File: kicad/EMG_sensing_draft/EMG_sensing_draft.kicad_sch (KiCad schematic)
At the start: 95 parts, among them J1 USB_A_0480370001, J2 EMG_SIGNAL, J3 DEBUG, U1 MCP6N11-002E/SN, U2 W25Q128JV, U3 ISL90462WIH627Z-TKCT-ND, U4 RP2040, U5 RN4871-I/RM140, U6 Opamp_MCP6024T-E/ST, U7 MCP1702T-3302E_CB, U8 MCP6021, U9 MCP6024T-E/ST, Y1 12MHz

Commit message: Edited multi-unit component
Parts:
- removed C20: 1uF, Capacitor_SMD:C_0603_1608Metric, symbol Device:C
- removed C21: 0.1uF, Capacitor_SMD:C_0603_1608Metric, symbol Device:C
- removed C22: 10uF, Capacitor_SMD:C_0603_1608Metric, symbol Device:C
- removed C23, C29: .33uF, Capacitor_SMD:C_0603_1608Metric, symbol Device:C
- removed C26: .033uF, Capacitor_SMD:C_0603_1608Metric, symbol Device:C
- removed D10, D9: D, symbol Device:D
- removed R19: 787, Resistor_SMD:R_0603_1608Metric, symbol Device:R
- removed R21, R36: 453, Resistor_SMD:R_0603_1608Metric, symbol Device:R
- removed R22, R34: 909, Resistor_SMD:R_0603_1608Metric, symbol Device:R
- removed R23: 8.1k, Resistor_SMD:R_0603_1608Metric, symbol Device:R
- removed R25: 9.09k, Resistor_SMD:R_0603_1608Metric, symbol Device:R
- removed R33, R37, R39, R40: 10k, symbol Device:R
- removed R38: R, symbol Device:R
- removed U9: MCP6024T-E/ST, MCP6024:MCP6024T, symbol MCP6024:MCP6024T-E/ST
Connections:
- net +1.65V: now also U6.12 (VINB+), U6.3 (VINA+); no longer U6.1 (VINA+), U6.1 (VINB+)
- net +3.3V: now also U6.4 (VDD); no longer U6. (VSS)
- net GND: now also C28.1, R32.1, U6.11 (VSS); no longer U6. (VSS)
- net Vout_1: now also U6.13 (VINB-); no longer D7.2 (A), R17.1
- net Vout_2_neg: now also U6.9 (VINC-); no longer U6.2 (VINC-)
- net Vout_2_pos: now also U6.10 (VINC+); no longer U6.1 (VINC+)
- net Vout_3: now also U6.8 (VOUTC); no longer U6.3 (VOUTC)
- net at R11.2, R12.1: now also U6.1 (VOUTA); no longer U6.3 (VOUTA)
- net at R14.2: now also D7.2 (A), R17.1; no longer U6.2 (VINB-)
- net at D7.1 (K), D8.2 (A): now also U6.14 (VOUTB); no longer U6.3 (VOUTB)
- net at C27.2, R31.2, R35.1: now also U6.7 (VOUTD); no longer C28.1, R32.1, U6.3 (VOUTD)
- net at C28.2, R30.2, R32.2: now also U6.5 (VIND+); no longer U6.1 (VIND+)
- net at C27.1, R29.2, R31.1: now also U6.6 (VIND-); no longer U6.2 (VIND-)
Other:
- note removed: "BANDPASS FILTER, RECTIFICATION, AND LEVEL SHIFTING 2"
- moved on the sheet: C15, C16, C17, C27, C28, C30, D7, D8, R10, R11, R12, R14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

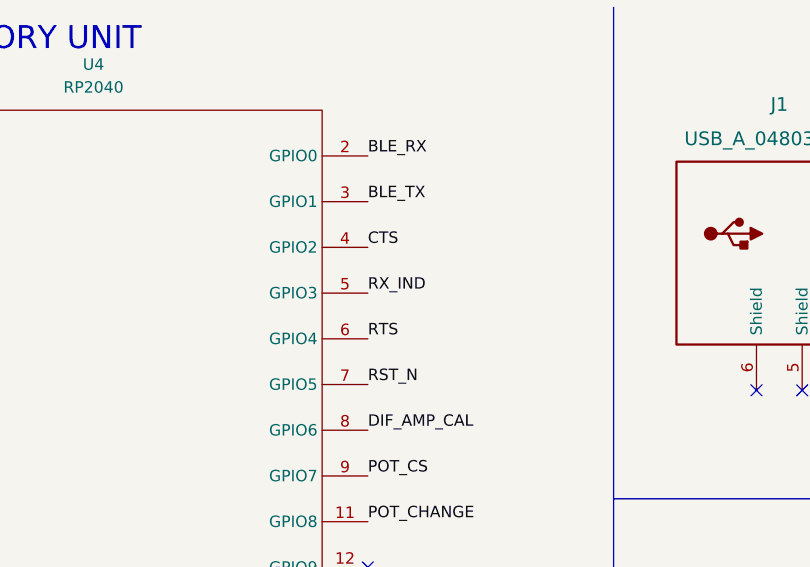
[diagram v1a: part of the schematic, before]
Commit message: fixed ble pins
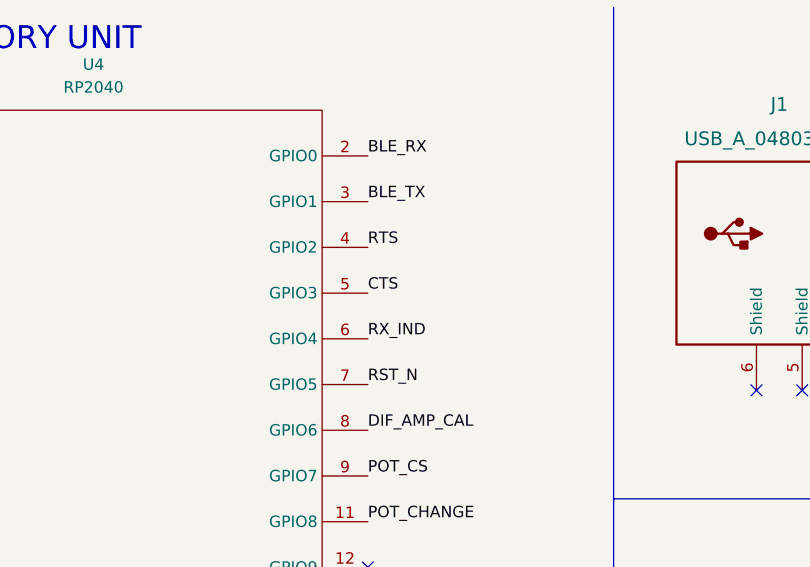
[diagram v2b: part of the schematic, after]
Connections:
- net CTS: now also U4.5 (GPIO3); no longer U4.4 (GPIO2)
- net RTS: now also U4.4 (GPIO2); no longer U4.6 (GPIO4)
- net RX_IND: now also U4.6 (GPIO4); no longer U4.5 (GPIO3)
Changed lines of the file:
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@@
     (effects (font (size 1.27 1.27)) (justify left bottom))
   )
-  (label "RTS" (at 137.16 49.53 0)
+  (label "RTS" (at 137.16 39.37 0)
     (effects (font (size 1.27 1.27)) (justify left bottom))
   )
@@
     (effects (font (size 1.27 1.27)) (justify right bottom))
   )
-  (label "CTS" (at 137.16 39.37 0)
+  (label "CTS" (at 137.16 44.45 0)
     (effects (font (size 1.27 1.27)) (justify left bottom))
   )
@@
     (effects (font (size 1.27 1.27)) (justify right bottom))
   )
-  (label "RX_IND" (at 137.16 44.45 0)
+  (label "RX_IND" (at 137.16 49.53 0)
     (effects (font (size 1.27 1.27)) (justify left bottom))
   )
@@
     (pin "3")
     (pin "10")
+    (pin "8")
     (pin "9")
-    (pin "8")
     (pin "1")
     (pin "2")
@@
     (pin "14")
     (pin "10")
+    (pin "8")
     (pin "9")
-    (pin "8")
     (pin "5")
     (pin "6")
     (pin "7")
+    (pin "11")
     (pin "4")
-    (pin "11")
   )
   (symbol (lib_id "power:+3.3V") (at 72.39 140.97 0) (unit 1)

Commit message: updated footprint assignments
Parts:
- C30: renamed from C25; value .1uF -> 0.1uF
- D7, D8: footprint (none) -> Diode_SMD:D_0805_2012Metric
- R18: renamed from R24; footprint (none) -> Resistor_SMD:R_0603_1608Metric
- R20: renamed from R12; footprint (none) -> Resistor_SMD:R_0603_1608Metric
- R21: renamed from R15; footprint (none) -> Resistor_SMD:R_0603_1608Metric
- R24: renamed from R14; footprint (none) -> Resistor_SMD:R_0603_1608Metric
- R30: renamed from R17; footprint (none) -> Resistor_SMD:R_0603_1608Metric
- U13: renamed from U6; footprint (none) -> MCP6024:MCP6024T
- renumbered C8 to C10, C9 to C11, C10 to C12, C11 to C13, C12 to C14, C13 to C15, C14 to C17, C18 to C22, C19 to C25, C15 to C26, C16 to C27, C17 to C28, C24 to C29, C1 to C3, C27 to C31, C28 to C32, C30 to C33, C2 to C4, C3 to C5, C4 to C6, C5 to C7, C6 to C8, C7 to C9, R9 to R10, R16 to R14, R10 to R15, R18 to R16, R20 to R17, R11 to R19, R29 to R22, R30 to R23, R26 to R25, R27 to R26, R28 to R27, R31 to R28, R32 to R29, R35 to R31, R5 to R6, R6 to R7, R7 to R8, R8 to R9, U7 to U11, U8 to U14, U1 to U2, U2 to U3, U3 to U5, U4 to U6, U5 to U9

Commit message: adde reformmated filtering symbol
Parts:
- added C? (x2): .33uF, Capacitor_SMD:C_0603_1608Metric, symbol Device:C
- added C?: 1uF, Capacitor_SMD:C_0603_1608Metric, symbol Device:C
- added C?: 0.1uF, Capacitor_SMD:C_0603_1608Metric, symbol Device:C
- added C?: .033uF, Capacitor_SMD:C_0603_1608Metric, symbol Device:C
- added C?: 10uF, Capacitor_SMD:C_0603_1608Metric, symbol Device:C
- added D? (x2): D, Diode_SMD:D_0805_2012Metric, symbol Device:D
- added R?: 787, Resistor_SMD:R_0603_1608Metric, symbol Device:R
- added R? (x2): 453, Resistor_SMD:R_0603_1608Metric, symbol Device:R
- added R?: 9.09k, Resistor_SMD:R_0603_1608Metric, symbol Device:R
- added R? (x5): 10k, Resistor_SMD:R_0603_1608Metric, symbol Device:R
- added R? (x2): 909, Resistor_SMD:R_0603_1608Metric, symbol Device:R
- added R?: 8.1k, Resistor_SMD:R_0603_1608Metric, symbol Device:R
- added U? (x5): Opamp_MCP6024T-E/ST, MCP6024:MCP6024T, symbol Device:Opamp_MCP6024T-E/ST
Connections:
- net +1.65V: now also R?.1, U?.12 (VINB+), U?.3 (VINA+)
- net +3.3V: now also C?.2, C?.2, U?.4 (VDD)
- net GND: now also C?.1, C?.1, C?.1, C?.2, R?.1, U?.11 (VSS)
- new net: C?.2, R?.2, R?.2, U?.5 (VIND+)
- new net: C?.1, R?.1, R?.2, U?.6 (VIND-)
- new net: C?.2, R?.1, R?.2, U?.7 (VOUTD)
- new net: D?.1 (K), D?.2 (A), U?.14 (VOUTB)
- new net: D?.2 (A), R?.1, R?.2
- new net: D?.1 (K), R?.2, U?.10 (VINC+)
- new net: R?.1, R?.1, R?.2, U?.13 (VINB-)
- new net: C?.1, R?.2
- new net: R?.1, R?.2, U?.8 (VOUTC)
- new net: R?.1, R?.2, U?.9 (VINC-)
- new net: R?.1, R?.2, U?.1 (VOUTA)
- new net: C?.2, R?.1, U?.2 (VINA-)
- new net V_DIFF_ONE: R?.1
- new net V_SIGNAL_TWO: C?.1, R?.2

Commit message: Add two channel schematics
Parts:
- removed C? (x2): .33uF, Capacitor_SMD:C_0603_1608Metric, symbol Device:C
- removed C?: 1uF, Capacitor_SMD:C_0603_1608Metric, symbol Device:C
- removed C?: 0.1uF, Capacitor_SMD:C_0603_1608Metric, symbol Device:C
- removed C?: .033uF, Capacitor_SMD:C_0603_1608Metric, symbol Device:C
- removed C?: 10uF, Capacitor_SMD:C_0603_1608Metric, symbol Device:C
- removed D? (x2): D, Diode_SMD:D_0805_2012Metric, symbol Device:D
- removed J2: EMG_SIGNAL, Connector_PinHeader_2.54mm:PinHeader_1x03_P2.54mm_Vertical, symbol Connector_Generic:Conn_01x03
- removed R?: 787, Resistor_SMD:R_0603_1608Metric, symbol Device:R
- removed R? (x2): 453, Resistor_SMD:R_0603_1608Metric, symbol Device:R
- removed R?: 9.09k, Resistor_SMD:R_0603_1608Metric, symbol Device:R
- removed R? (x5): 10k, Resistor_SMD:R_0603_1608Metric, symbol Device:R
- removed R? (x2): 909, Resistor_SMD:R_0603_1608Metric, symbol Device:R
- removed R?: 8.1k, Resistor_SMD:R_0603_1608Metric, symbol Device:R
- removed U11: MCP1702T-3302E_CB, Package_TO_SOT_SMD:SOT-23, symbol Eclectronics:MCP1702T-3302E_CB
- removed U13, U? (x5): Opamp_MCP6024T-E/ST, MCP6024:MCP6024T, symbol Device:Opamp_MCP6024T-E/ST
- removed U14: MCP6021, Package_TO_SOT_SMD:SOT-23-5, symbol Eclectronics:MCP6021
- removed U9: RN4871-I/RM140, RN4871:RN4871, symbol RN4871:RN4871-I/RM140
- added C1, C2, C20, C21: 1uF, Capacitor_SMD:C_0603_1608Metric, symbol Device:C
- added C16, C23: 0.1uF, Capacitor_SMD:C_0603_1608Metric, symbol Device:C
- added C18, C19, C24: 10uF, Capacitor_SMD:C_0603_1608Metric, symbol Device:C
- added D10, D9: D, Diode_SMD:D_0805_2012Metric, symbol Device:D
- added J2: Conn_01x05, symbol Connector_Generic:Conn_01x05
- added R11, R12: 1k, Resistor_SMD:R_0603_1608Metric, symbol Device:R
- added R32, R33: 10k, Resistor_SMD:R_0603_1608Metric, symbol Device:R
- added R34, R35, R36, R37: 453, Resistor_SMD:R_0603_1608Metric, symbol Device:R
- added R38, R39, R40, R41: 909, Resistor_SMD:R_0603_1608Metric, symbol Device:R
- added R42, R43: 9.09k, Resistor_SMD:R_0603_1608Metric, symbol Device:R
- added R5: 100k, Resistor_SMD:R_0603_1608Metric, symbol Device:R
- added U1: MCP6N11-002E/SN, MCP6N11:MCP6N11-002ESN, symbol MCP6N11:MCP6N11-002E/SN
- added U10, U9: Opamp_MCP6024T-E/ST, MCP6024:MCP6024T, symbol Device:Opamp_MCP6024T-E/ST
- added U11: MCP6021, Package_TO_SOT_SMD:SOT-23-5, symbol Eclectronics:MCP6021
- added U4: ISL90462WIH627Z-TKCT-ND, ISL90462WIH627Z:ISL90462WIH627Z-TKCT-ND, symbol ISL90462WIH627Z-TKCT-ND:ISL90462WIH627Z-TKCT-ND
- added U7: RN4871-I/RM140, RN4871:RN4871, symbol RN4871:RN4871-I/RM140
- added U8: MCP1702T-3302E_CB, Package_TO_SOT_SMD:SOT-23, symbol Eclectronics:MCP1702T-3302E_CB
- C22: value 10uF -> 0.1uF
- C28: value 10uF -> .33uF
- C29: value 1uF -> .33uF
- C3: value 1uF -> 0.1uF
- C30: value 0.1uF -> .33uF
- C32: value .33uF -> .033uF
- R13, R14: value 1k -> 787
- R15: value 787 -> 10k
- R17, R18: value 10k -> 8.1k
- R19: value 8.1k -> 10k
- R22, R23: value 453 -> 10k
- R28, R29: value 909 -> 100k
- R31: value 9.09k -> 10k
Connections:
- net +1.65V: now also R34.1, R36.1, U1.5 (VREF), U10.12 (VINB+), U10.3 (VINA+), U11.1, U11.4, U4.5 (RW), U9.12 (VINB+), U9.3 (VINA+); no longer R22.1
- net +3.3V: now also C22.2, C26.1, C27.1, C3.2, C4.1, R15.1, C1.1, C16.1, C19.1, C2.1, C20.2, C21.2, C23.2, R12.1, U1.7 (VDD), U10.4 (VDD), U11.5, U4.1 (VDD), U7.14 (VBAT), U8.2 (VOUT), U9.4 (VDD); no longer C25.1, C26.2, C27.2, C29.1, C3.1, C30.1, C4.2, R14.1, R16.1
- net BLE_RX: now also U7.7 (UART_RX)
- net BLE_TX: now also U7.8 (UART_TX)
- net CTS: now also U7.11 (P0_0)
- net GND: now also C26.2, C27.2, C29.1, C3.1, C31.1, C32.2, C4.2, R16.1, C1.2, C16.2, C18.1, C19.2, C2.2, C20.1, C21.1, C23.1, R39.1, R41.1, U1.4 (VSS), U10.11 (VSS), U11.2, U4.2 (GND), U7.13 (GND), U7.2 (GND), U8.1 (GND), U9.11 (VSS); no longer C25.2, C26.1, C27.1, C29.2, C3.2, C30.2, C32.1, C4.1, R17.1, R29.1
- net RST_N: now also U7.10 (RST_N)
- net RTS: now also U7.9 (P3_6)
- net RX_IND: now also U7.6 (P1_6)
- net V_DIFF_ONE: now also R13.1, R6.1, U2.6 (VOUT)
- net V_SIGNAL_TWO: now also C32.1, C33.1, U6.39 (GPIO27/ADC1), R42.2, R43.2
- net at R19.1: now also R17.2, U9.1 (VOUTA); no longer C28.2
- net at R19.2: now also R21.1, R23.1, U9.13 (VINB-); no longer R20.1
- net POT_CS_ONE: now reaches U6.13 (GPIO10)
- net POT_CS_ONE: now also U5.4 (*CS)
- net POT_CHANGE_ONE: now reaches U6.14 (GPIO11)
- net POT_CHANGE_ONE: now also U5.3 (U/*D)
- net POT_CS_TWO: now reaches U6.15 (GPIO12)
- net POT_CS_TWO: now also U4.4 (*CS)
- net POT_CHANGE_TWO: now reaches U6.16 (GPIO13)
- net POT_CHANGE_TWO: now also U4.3 (U/*D)
- net V_SIGNAL_ONE: now reaches U6.38 (GPIO26/ADC0)
- net at R16.2: now also R15.2, U11.3; no longer R17.2
- net at R14.2: now also C25.1; no longer D6.2 (A)
- net at J1.1 (VBUS): now also C18.2, U8.3 (VIN); no longer C22.2
- net at C28.1: now also R34.2, R38.1, U9.6 (VIND-); no longer R15.2
- net at D7.2 (A), R30.1: now also R23.2; no longer R24.2
- net at D7.1 (K), D8.2 (A): now also U9.14 (VOUTB)
- net at R25.1: now also J2.1 (Pin_1)
- net at D5.1 (K): now also R11.2; no longer R13.2
- net at R26.1: now also J2.2 (Pin_2)
- net at R27.1: now also J2.3 (Pin_3)
- net DIF_AMP_CAL renamed DIF_AMP_ONE_CAL
- net POT_CHANGE: no longer names the net of U6.11 (GPIO8)
- net POT_CHANGE: no longer U5.3 (U/*D)
- net POT_CS renamed DIF_AMP_TWO_CAL
- net DIF_AMP_TWO_CAL: now also U1.8 (EN/*CAL); no longer U5.4 (*CS)
- removed net V_DIFF: R15.1, R6.1, U2.6 (VOUT)
- removed net V_SIGNAL: C33.1, R31.2, U6.41 (GPIO29/ADC3)
- net Vout_1: no longer names the net of R20.2, R24.1
- net Vout_1: now also R22.1, U10.13 (VINB-); no longer R21.1
- net Vout_2_neg: no longer names the net of R18.1
- net Vout_2_neg: now also C25.2, U10.2 (VINA-); no longer R30.2
- net Vout_2_pos: no longer names the net of D8.1 (K), R21.2
- net Vout_2_pos: now also U9.10 (VINC+)
- net Vout_3: no longer names the net of R18.2
- net Vout_3: now also R20.1, U10.1 (VOUTA); no longer R23.1
- net emg_node_one renamed EMG_NODE_ONE
- net EMG_NODE_ONE: now also R25.2; no longer R26.2
- net emg_node_two renamed EMG_NODE_TWO
- net EMG_NODE_TWO: now also R26.2; no longer R25.2
- net emg_ref renamed EMG_NODE_THREE
- net EMG_NODE_THREE: now also U1.2 (VIM)
- new net: J2.5 (Pin_5), R29.1
- new net: C29.2, R35.2, R39.2, U9.5 (VIND+)
- new net: C30.1, R36.2, R40.1, U10.6 (VIND-)
- new net: D10.2 (A), D9.1 (K), U10.14 (VOUTB)
- new net: R11.1, U7.12 (P0_2)
- new net: J2.4 (Pin_4), R28.1
- new net: R33.2, R37.1, U10.8 (VOUTC)
- new net: C31.2, R37.2, R41.2, U10.5 (VIND+)
- new net: C24.1, R13.2
- new net: C30.2, R40.2, R43.1, U10.7 (VOUTD)
- new net: R5.2, U1.1 (VFG), U4.6 (RH)
- new net: D6.2 (A), R12.2
- new net: R30.2, R32.1, U9.9 (VINC-)
- new net: R32.2, R35.1, U9.8 (VOUTC)
- new net: C24.2, R17.1, U9.2 (VINA-)
- new net: D10.1 (K), R22.2, U10.10 (VINC+)
- new net: R31.2, R33.1, U10.9 (VINC-)
- new net: D9.2 (A), R24.2, R31.1
- new net: C28.2, R38.2, R42.1, U9.7 (VOUTD)
- new net EMG_NODE_FOUR: R28.2, U1.3 (VIP)
- new net EMG_REF: R29.2
- new net V_DIFF_TWO: R14.1, R5.1, U1.6 (VOUT)
- no-connect marks 23 -> 11
